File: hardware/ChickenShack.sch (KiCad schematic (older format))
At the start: 37 parts, among them P1 BATTERY, P2 LIGHT, P3 D_SWITCH, P4 D_SENSOR, P5 DEBUG, P6 D_MOTOR, P7 SCOPE, Q1 MOSFET_P, Q2 MOSFET_N, U1 MAX604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

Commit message: AVCC and AREF connections were reversed on the schematic (the tracks were cut and connections bodged on the original PCB order)
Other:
- note added: "TODO:"
- note removed: "TODO: FIX PIN ASSIGNMENT"
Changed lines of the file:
@@
-EESchema Schematic File Version 2  date Wed 01 Sep 2010 22:07:03 BST
+EESchema Schematic File Version 2  date Sun 30 Dec 2012 09:07:04 GMT
 LIBS:power
 LIBS:device
@@
 LIBS:XBee
 LIBS:ChickenShack-cache
-EELAYER 24  0
+EELAYER 25  0
 EELAYER END
 $Descr A4 11700 8267
+encoding utf-8
 Sheet 1 1
 Title ""
-Date "1 sep 2010"
+Date "30 dec 2012"
 Rev ""
 Comp ""
@@
 Comment4 ""
 $EndDescr
+Connection ~ 10700 2650
+Wire Wire Line
+	9350 2650 10700 2650
 Wire Wire Line
 	7700 1000 7650 1000
@@
 Wire Wire Line
 	10700 3700 10700 3450
-Connection ~ 10700 2550
 Connection ~ 10250 3700
 Wire Wire Line
@@
 	6800 2550 6800 3850
 Wire Wire Line
-	10450 3050 10450 2650
-Wire Wire Line
-	10450 2650 9350 2650
-Wire Wire Line
 	10700 1650 10700 1050
 Wire Wire Line
 	10700 3050 10700 2250
-Wire Wire Line
-	9350 2550 10700 2550
 Wire Wire Line
 	7650 5200 7250 5200
@@
 Wire Wire Line
 	9350 1050 9750 1050
+Wire Wire Line
+	10450 3050 10450 2550
+Wire Wire Line
+	10450 2550 9350 2550
 $Comp
 L R R2
@@
 M_ENABLE
 Text Notes 9050 3500 0    50   ~ 0
-TODO: FIX PIN ASSIGNMENT
+TODO:
 Text GLabel 9700 2950 2    50   Input ~ 0
 UP

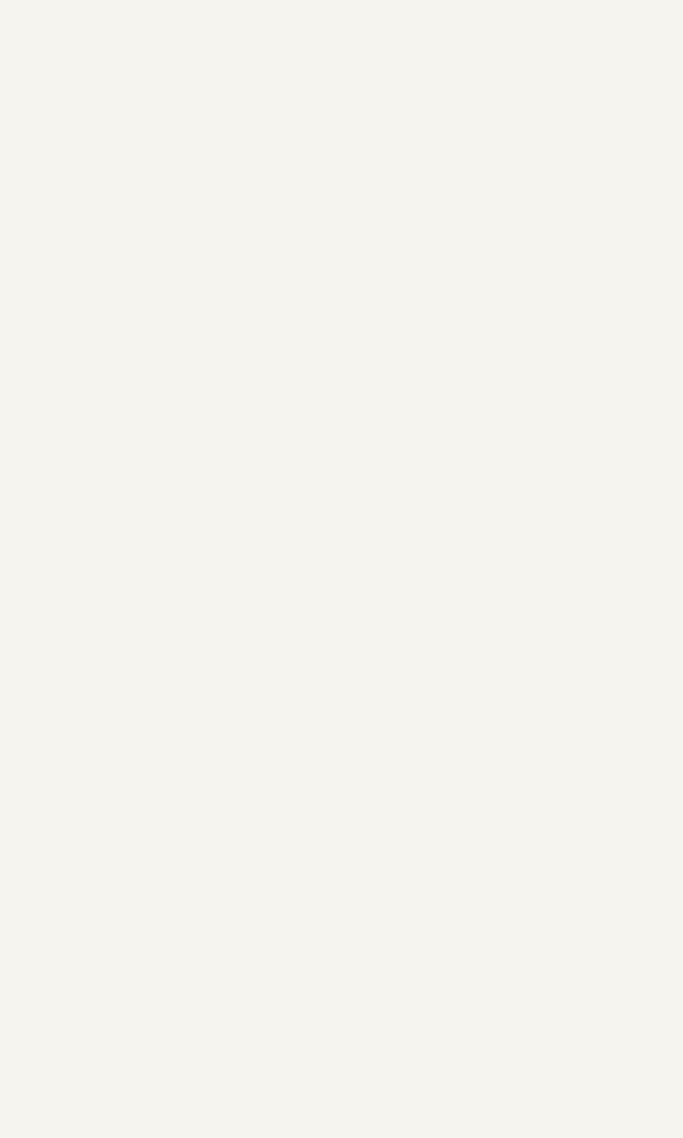
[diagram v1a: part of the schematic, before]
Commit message: Start migration to SMD components, replace MCU & LDO in schematic
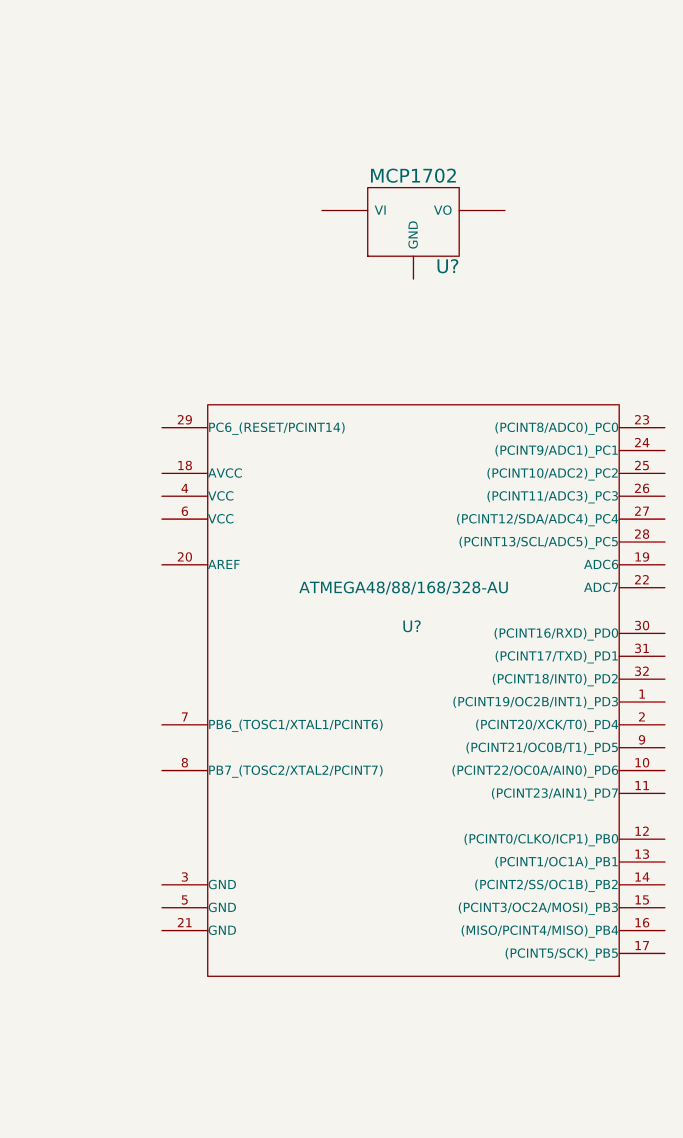
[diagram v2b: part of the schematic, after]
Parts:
- added U?: MCP1702, symbol MCP1702
- added U?: ATMEGA48/88/168/328-AU, symbol ATMEGA48/88/168/328-AU
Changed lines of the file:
@@
-EESchema Schematic File Version 2  date Sun 30 Dec 2012 09:07:04 GMT
-LIBS:power
-LIBS:device
-LIBS:transistors
-LIBS:conn
-LIBS:linear
-LIBS:regul
-LIBS:74xx
-LIBS:cmos4000
-LIBS:adc-dac
-LIBS:memory
-LIBS:xilinx
-LIBS:special
-LIBS:microcontrollers
-LIBS:dsp
-LIBS:microchip
-LIBS:analog_switches
-LIBS:motorola
-LIBS:texas
-LIBS:intel
-LIBS:audio
-LIBS:interface
-LIBS:digital-audio
-LIBS:philips
-LIBS:display
-LIBS:cypress
-LIBS:siliconi
-LIBS:opto
-LIBS:atmel
-LIBS:contrib
-LIBS:valves
-LIBS:max604
-LIBS:atmega88-pa
-LIBS:tb6612fng_mod
-LIBS:XBee
+EESchema Schematic File Version 2  date Mon 31 Dec 2012 10:18:49 GMT
+LIBS:dresco
 LIBS:ChickenShack-cache
 EELAYER 25  0
@@
 Sheet 1 1
 Title ""
-Date "30 dec 2012"
+Date "31 dec 2012"
 Rev ""
 Comp ""
@@
 Comment4 ""
 $EndDescr
+$Comp
+L ATMEGA48/88/168/328-AU U?
+U 1 1 50E16640
+P 12950 3400
+F 0 "U?" H 12900 3500 50  0000 L BNN
+F 1 "ATMEGA48/88/168/328-AU" H 12450 3670 50  0000 L BNN
+	1    12950 3400
+	1    0    0    -1
+$EndComp
+$Comp
+L MCP1702 U?
+U 1 1 50E16625
+P 12950 1500
+F 0 "U?" H 13100 1304 60  0000 C CNN
+F 1 "MCP1702" H 12950 1700 60  0000 C CNN
+	1    12950 1500
+	1    0    0    -1
+$EndComp
 Connection ~ 10700 2650
 Wire Wire Line

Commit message: More schematic changes for SMD components, various pin changes to accomodate ISP header etc
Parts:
- removed P2: LIGHT, symbol CONN_2
- removed P3: D_SWITCH, symbol CONN_4
- removed P4: D_SENSOR, symbol CONN_4
- removed P5: DEBUG, symbol CONN_2
- removed Q1: MOSFET_P, symbol MOSFET_P
- removed Q2: MOSFET_N, symbol MOSFET_N
- removed U1: MAX604, symbol MAX604
- removed U2: ATMEGA88-PA, symbol ATMEGA88-PA
- removed U?: ATMEGA48/88/168/328-AU, symbol ATMEGA48/88/168/328-AU
- added C8: 0.1uF, symbol C
- added ISP?: AVR-ISP-6, AVR-ISP-6, symbol AVR-ISP-6
- added P4: LIGHT, symbol CONN_2
- added P5: D_SWITCH, symbol CONN_4
- added P6: D_SENSOR, symbol CONN_4
- added P7: DEBUG, symbol CONN_2
- added P?: SPARE, symbol CONNECTOR
- added Q1: MOSFET_N, symbol MOSFET_N
- added Q2: MOSFET_P, symbol MOSFET_P
- added U2: ATMEGA88-AU, symbol ATMEGA48/88/168/328-AU
- C3, C5, C7: value C -> 0.1uF
- C4, C6: value C -> 22pF
- R2: value 4.7K -> 10K
- R4: value 10K -> 4.7K
- gave numbers to parts that had none: 1
- renumbered MOD2 to MOD1, MOD1 to MOD2, P6 to P2, P7 to P3
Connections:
- net labels added: MISO, MOSI, RST, SCK, SCOPE, SPARE
- wire segments 169 -> 218
- no-connect marks 16 -> 14
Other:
- note added: "Check mosfet circuit"
- note added: "In System Programming"
- note added: "Motor driver"
- note added: "Power supply"
- note added: "TODO:\nPin reassignments to accomodate ISP connections (PBx)\n\nFROM TO ASSIGNMENT\n----------------------------------\nPB0 PC4 SCOPE - DEBUG OUTPUT\nPB1 PB0 PW\nPB2 PC1 RADIO_SLEEP\nPB3 PB1 UP\nPB4 PC2 RADIO_CTS\nPB5 PB2 DOWN\nPC0 PC5 Light Sensor\nPC1 ADC6 Trim pot\nPC2 ADC7 Battery voltage\nPC5 PC0 enable ADC inputs\n PC3 SPARE (possible future microswitch)\n\n\n"
- note added: "Voltage divider for battery ADC input"
- note added: "XBee radio module"
- note removed: "TODO:"
- moved on the sheet: D1, D2, D3, D4, D5, D6, D7, D8, MOD1, P1, P2, U1

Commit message: SMD schematic and netlist updates
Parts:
- removed C1, C2: CP1, symbol CP1
- removed MOD2: XBEE-00, XBee-00, symbol XBEE-00
- removed P3: SCOPE, symbol CONNECTOR
- removed P?: SPARE, symbol CONNECTOR
- added C1, C2: 1uF, symbol C
- added MOD2: XBEE, XBee, symbol XBEE
- added P2, P3: CONN_1, symbol CONN_1
- gave numbers to parts that had none: 1
- renumbered P7 to P4, P2 to P5, P4 to P6, P6 to P7, P5 to P8
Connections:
- net labels added: DEBUG
- wire segments 218 -> 169
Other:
- note added: "Debug / Probe / Spare pins"
- note added: "Enable voltage dividers"
- note added: "Light sensor \nvoltage divider"
- note added: "NOTES:\n\nPin reassignments to accomodate ISP connections (PBx)\n\nFROM TO ASSIGNMENT\n----------------------------------\nPB0 PC4 SCOPE - DEBUG OUTPUT\nPB1 PB0 PW\nPB2 PC1 RADIO_SLEEP\nPB3 PB1 UP\nPB4 PC2 RADIO_CTS\nPB5 PB2 DOWN\nPC0 PC5 Light Sensor\nPC1 ADC6 Trim pot\nPC2 ADC7 Battery voltage\nPC5 PC0 enable ADC inputs\n PC3 SPARE (possible future microswitch)\n\n\n"
- note added: "Note: External flyback diodes should not\nbe necessary with TB6612FNG design, \nas there are internal protection diodes in \nthe package. Put footprints on the board\nbut not necessarily populated"
- note added: "Reference \nvoltage divider"
- note added: "Voltage divider for battery ADC input\n(VBatt is greater than Vcc)"
- note removed: "Check mosfet circuit"
- note removed: "TODO:\nPin reassignments to accomodate ISP connections (PBx)\n\nFROM TO ASSIGNMENT\n----------------------------------\nPB0 PC4 SCOPE - DEBUG OUTPUT\nPB1 PB0 PW\nPB2 PC1 RADIO_SLEEP\nPB3 PB1 UP\nPB4 PC2 RADIO_CTS\nPB5 PB2 DOWN\nPC0 PC5 Light Sensor\nPC1 ADC6 Trim pot\nPC2 ADC7 Battery voltage\nPC5 PC0 enable ADC inputs\n PC3 SPARE (possible future microswitch)\n\n\n"
- note removed: "Voltage divider for battery ADC input"
- moved on the sheet: C3, C4, C5, C6, C7, C8, D1, D2, D3, D4, D5, D6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

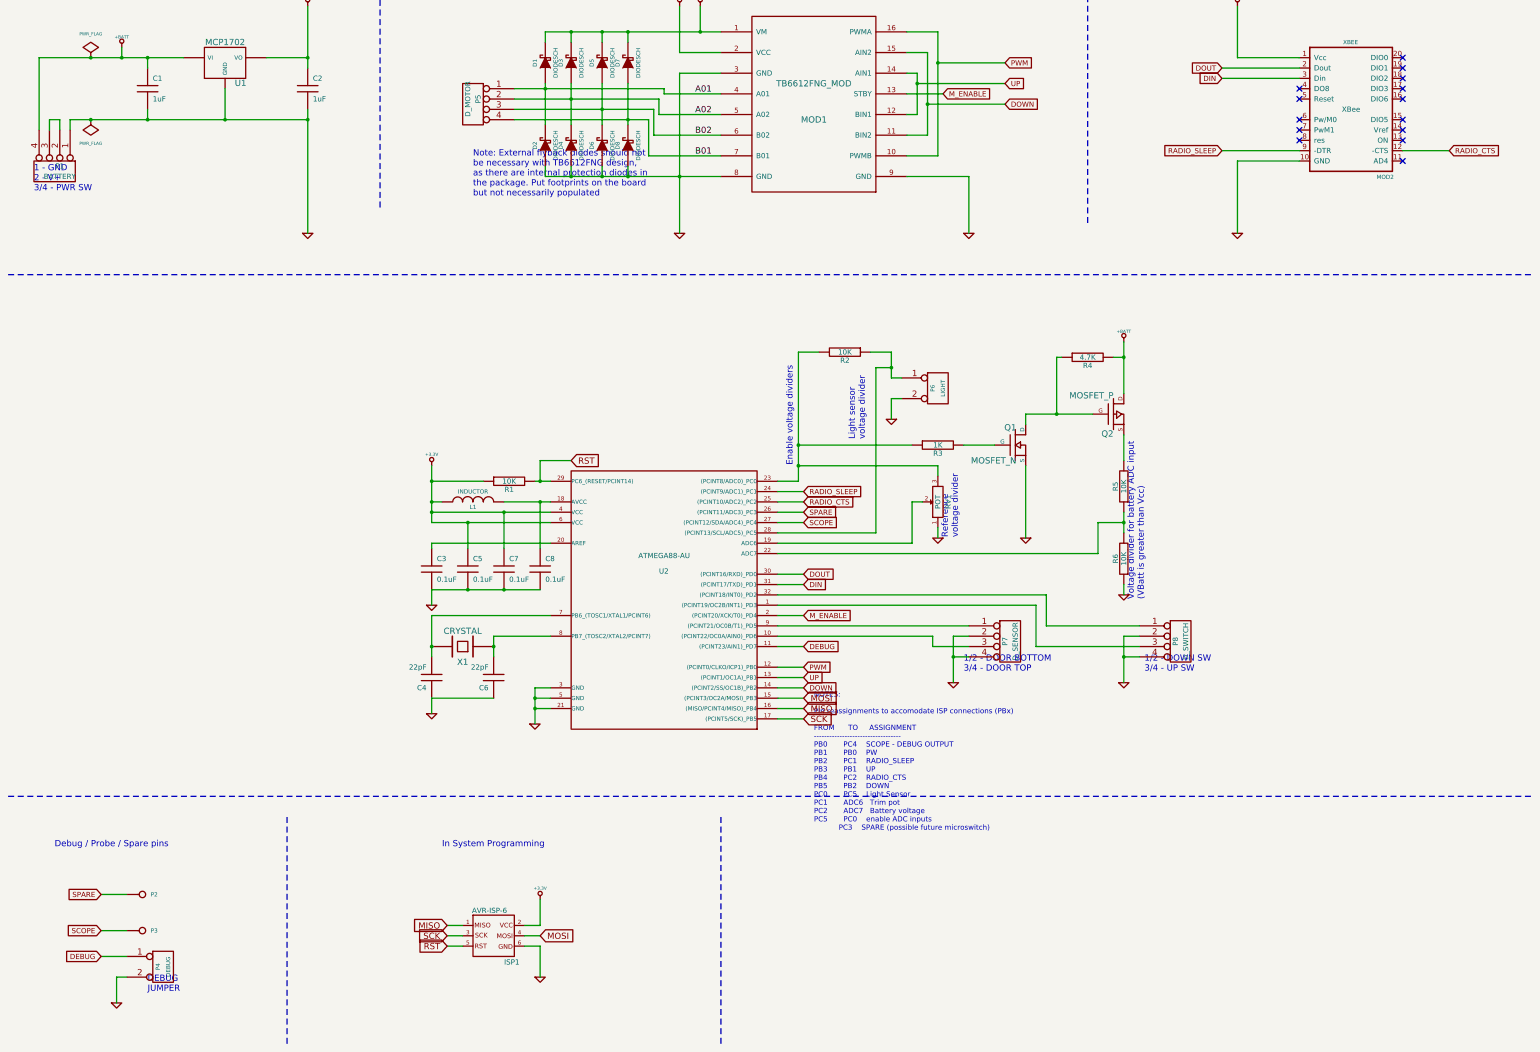
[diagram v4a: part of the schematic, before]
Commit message: Schematic tweaks, netlist footprint mappings, start new board layout
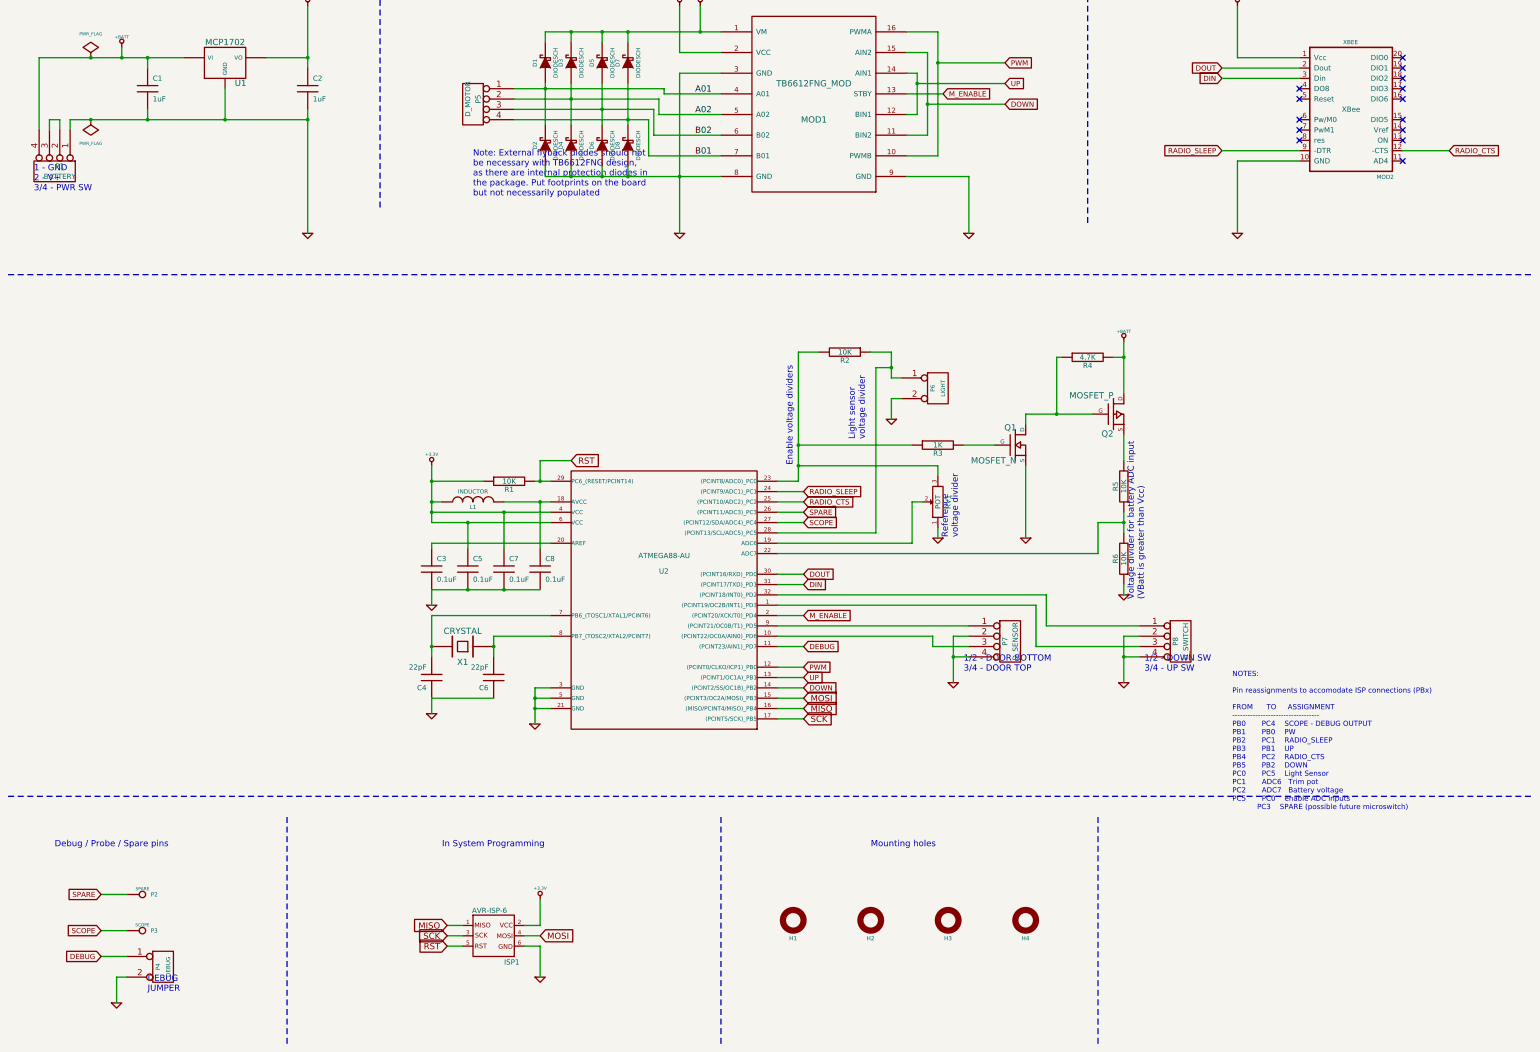
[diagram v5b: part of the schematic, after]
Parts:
- added H1, H2, H3, H4: HOLE, symbol HOLE
- P2: value CONN_1 -> SPARE
- P3: value CONN_1 -> SCOPE
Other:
- note added: "Mounting holes"
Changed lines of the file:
@@
-EESchema Schematic File Version 2  date Tue 01 Jan 2013 13:43:58 GMT
+EESchema Schematic File Version 2  date Wed 02 Jan 2013 22:36:13 GMT
 LIBS:dresco
 LIBS:ChickenShack-cache
@@
 Sheet 1 1
 Title ""
-Date "1 jan 2013"
+Date "2 jan 2013"
 Rev "2.00"
 Comp ""
@@
 $EndDescr
 $Comp
+L HOLE H4
+U 1 1 50E489AE
+P 10750 9850
+F 0 "H4" H 10710 9675 40  0000 L CNN
+F 1 "HOLE" H 10750 10020 30  0001 C CNN
+	1    10750 9850
+	1    0    0    -1
+$EndComp
+$Comp
+L HOLE H3
+U 1 1 50E489AA
+P 10000 9850
+F 0 "H3" H 9960 9675 40  0000 L CNN
+F 1 "HOLE" H 10000 10020 30  0001 C CNN
+	1    10000 9850
+	1    0    0    -1
+$EndComp
+$Comp
+L HOLE H2
+U 1 1 50E489A6
+P 9250 9850
+F 0 "H2" H 9210 9675 40  0000 L CNN
+F 1 "HOLE" H 9250 10020 30  0001 C CNN
+	1    9250 9850
+	1    0    0    -1
+$EndComp
+$Comp
+L HOLE H1
+U 1 1 50E4899F
+P 8500 9850
+F 0 "H1" H 8460 9675 40  0000 L CNN
+F 1 "HOLE" H 8500 10020 30  0001 C CNN
+	1    8500 9850
+	1    0    0    -1
+$EndComp
+Text Notes 9250 9150 0    60   ~ 0
+Mounting holes
+Wire Notes Line
+	11450 8850 11450 11050
+$Comp
 L CONN_1 P3
 U 1 1 50E2E7E8
 P 2200 9950
 F 0 "P3" H 2280 9950 40  0000 L CNN
-F 1 "CONN_1" H 2200 10005 30  0001 C CNN
+F 1 "SCOPE" H 2200 10005 30  0000 C CNN
 	1    2200 9950
 	1    0    0    -1
@@
 P 2200 9600
 F 0 "P2" H 2280 9600 40  0000 L CNN
-F 1 "CONN_1" H 2200 9655 30  0001 C CNN
+F 1 "SPARE" H 2200 9655 30  0000 C CNN
 	1    2200 9600
 	1    0    0    -1
@@
 	8600 7200 8350 7200
 Wire Wire Line
-	9450 4350 9250 4350
+	9250 4350 9450 4350
 Wire Wire Line
 	9450 5000 9450 4800
@@
 Connection ~ 11050 4950
 Wire Wire Line
-	11050 4400 11050 4950
+	11050 4950 11050 4400
 Wire Wire Line
 	11050 4400 11100 4400
@@
 	6050 10100 6050 10400
 Wire Wire Line
-	9450 4600 9550 4600
+	9550 4600 9450 4600
 Wire Wire Line
 	10450 5250 10150 5250
@@
 	5600 7700 5000 7700
 Wire Wire Line
-	6000 7600 6150 7600
+	6150 7600 6000 7600
 Connection ~ 5600 7200
 Wire Wire Line
@@
 	5600 7100 6150 7100
 Wire Wire Line
-	5000 6650 5000 6800
+	5000 6800 5000 6650
 Connection ~ 5700 6650
 Wire Wire Line
@@
 	5500 5600 5000 5600
 Wire Wire Line
-	5000 6000 5000 5450
-Wire Wire Line
-	6150 6000 5000 6000
+	5000 5450 5000 6000
+Wire Wire Line
+	5000 6000 6150 6000
 Wire Wire Line
 	6150 5600 6000 5600
@@
 	6150 5800 5700 5800
 Wire Wire Line
-	6000 7950 6000 7600
+	6000 7600 6000 7950
 Wire Wire Line
 	6150 7800 6000 7800
 Connection ~ 6000 7800
 Wire Wire Line
-	6050 6650 5000 6650
+	5000 6650 6050 6650
 Connection ~ 5350 6650
 Wire Wire Line
-	5000 6900 6150 6900
-Wire Wire Line
-	5000 7300 5000 6900
+	6150 6900 5000 6900
+Wire Wire Line
+	5000 6900 5000 7300
 Connection ~ 5000 7200
 Wire Wire Line
@@
 Connection ~ 6050 5600
 Wire Wire Line
-	1500 2100 1500 2200
+	1500 2200 1500 2100
 Wire Wire Line
 	1500 2100 3800 2100
@@
 	6350 2550 6350 2650
 Wire Wire Line
-	6100 2650 6100 2550
+	6100 2550 6100 2650
 Connection ~ 6900 1250
 Wire Wire Line
@@
 	6350 1250 6350 1350
 Wire Wire Line
-	9900 2450 9600 2450
+	9600 2450 9900 2450
 Wire Wire Line
 	9900 2450 9900 1250
@@
 	9900 1250 9600 1250
 Wire Wire Line
-	9700 2050 9600 2050
+	9600 2050 9700 2050
 Wire Wire Line
 	9700 2050 9700 1650
@@
 Connection ~ 2250 2100
 Wire Wire Line
-	7400 1650 7800 1650
-Wire Wire Line
-	7400 3200 7400 1650
+	7800 1650 7400 1650
+Wire Wire Line
+	7400 1650 7400 3200
 Wire Wire Line
 	9600 2650 10200 2650
@@
 	7400 1450 7400 1000
 Wire Wire Line
-	9800 2250 9600 2250
+	9600 2250 9800 2250
 Wire Wire Line
 	9800 2250 9800 1450
@@
 Connection ~ 6650 1250
 Wire Wire Line
-	7800 2650 6100 2650
+	6100 2650 7800 2650
 Wire Wire Line
 	6650 2650 6650 2550
@@
 	7800 2050 7200 2050
 Wire Wire Line
-	7200 1900 7200 2050
-Wire Wire Line
-	5800 1900 7200 1900
+	7200 2050 7200 1900
+Wire Wire Line
+	7200 1900 5800 1900
 Connection ~ 6100 1800
 Connection ~ 6350 1900
@@
 	11850 7000 10950 7000
 Wire Wire Line
-	11700 7100 11850 7100
-Wire Wire Line
-	11700 7550 11700 7100
+	11850 7100 11700 7100
+Wire Wire Line
+	11700 7100 11700 7550
 Wire Wire Line
 	9900 6050 9900 6150
@@
 	9650 6200 8350 6200
 Wire Wire Line
-	8550 5600 8350 5600
+	8350 5600 8550 5600
 Wire Wire Line
 	8350 7500 8600 7500
@@
 	10750 4950 10750 5050
 Wire Wire Line
-	9450 4350 9450 4600
+	9450 4600 9450 4350
 Wire Wire Line
 	8550 5600 8550 4350
@@
 Text GLabel 9950 1850 2    50   Input ~ 0
 M_ENABLE
-Text Notes 8700 9150 0    50   ~ 0
+Text Notes 12750 8950 0    50   ~ 0
 NOTES:\n\nPin reassignments to accomodate ISP connections (PBx)\n\nFROM      TO     ASSIGNMENT\n----------------------------------\nPB0       PC4    SCOPE - DEBUG OUTPUT\nPB1       PB0    PW\nPB2       PC1    RADIO_SLEEP\nPB3       PB1    UP\nPB4       PC2    RADIO_CTS\nPB5       PB2    DOWN\nPC0       PC5    Light Sensor\nPC1       ADC6   Trim pot\nPC2       ADC7   Battery voltage\nPC5       PC0    enable ADC inputs\n           PC3    SPARE (possible future microswitch)\n\n\n
 Text GLabel 8600 7500 2    50   Input ~ 0

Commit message: More layout
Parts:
- removed P2: SPARE, symbol CONN_1
- added P2: D_SENSE2, symbol CONN_2
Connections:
- net GND: now also P2.2 (PM)
- net SPARE renamed D_SENSE2
- net D_SENSE2: now also P2.1 (P1)
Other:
- note added: "DOOR TENSION\nMICRO SWITCH"
- moved on the sheet: P3, P4
